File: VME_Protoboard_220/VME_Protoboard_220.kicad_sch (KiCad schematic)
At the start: 55 parts, among them J1 Conn_02x08_Odd_Even, J2 Conn_02x08_Odd_Even, J3 Conn_02x12_Odd_Even, J4 Conn_02x07_Odd_Even, U1 74x16245, U2 74x16245, U3 74x16245, U4 74x1G19, U5 74x1G07, U6 74x1G07, U7 74x1G125, U8 74x1G125, U9 74x1G125, X1 DIN41612_03x32_ABC_VMEbus

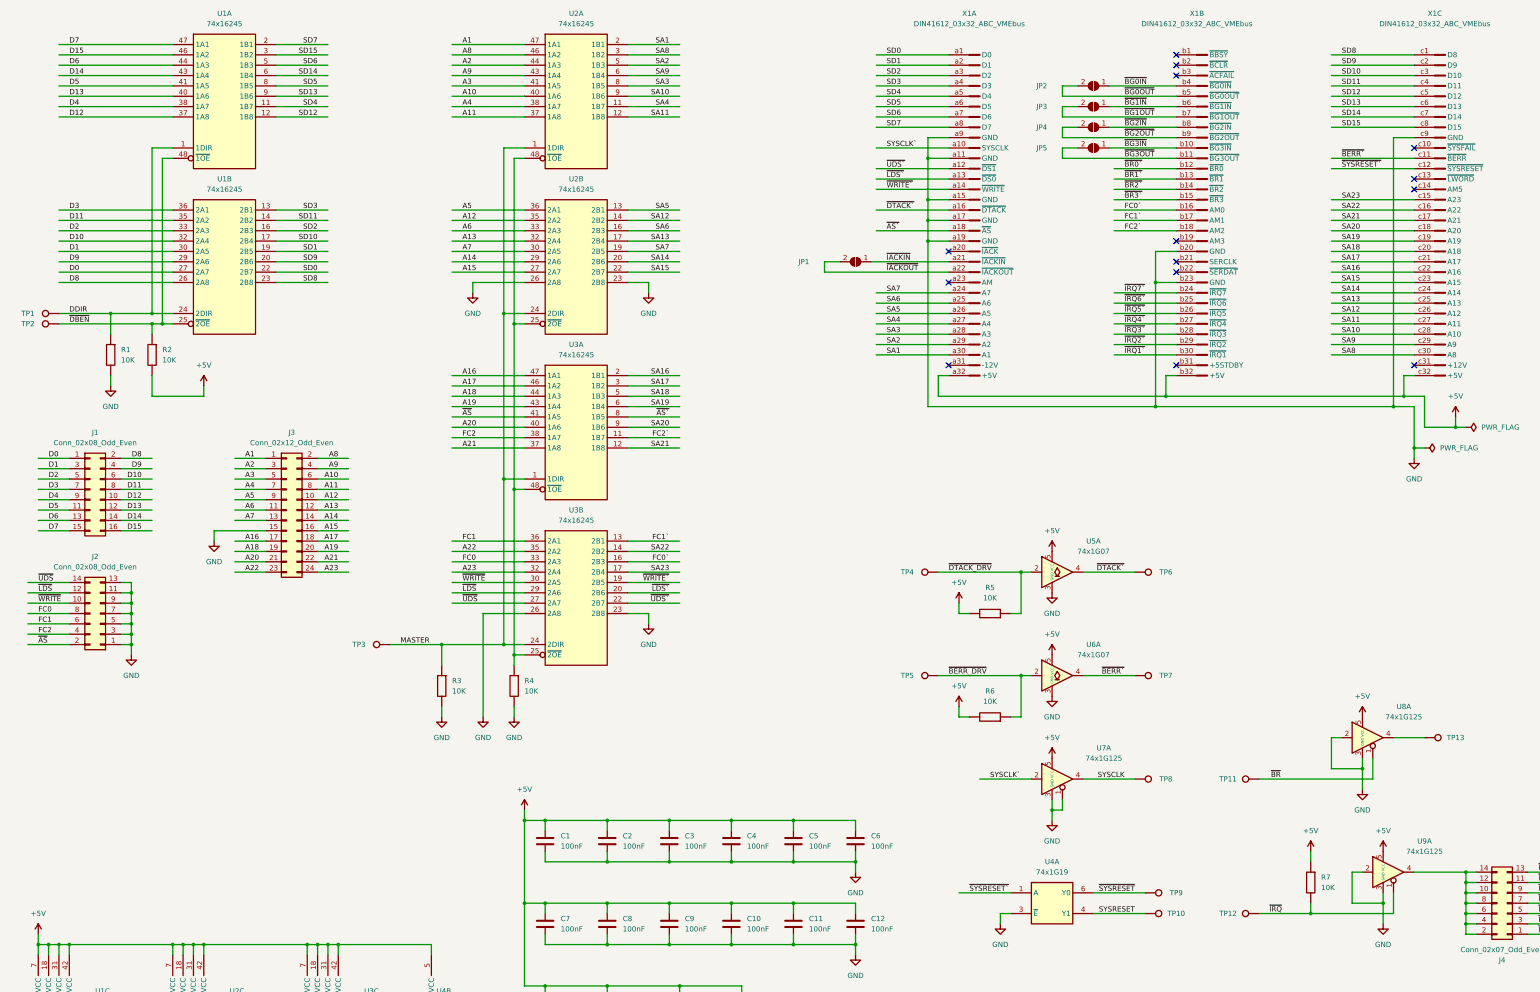
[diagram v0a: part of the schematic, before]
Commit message: Add extra test point for independent output control of each half of the data bus
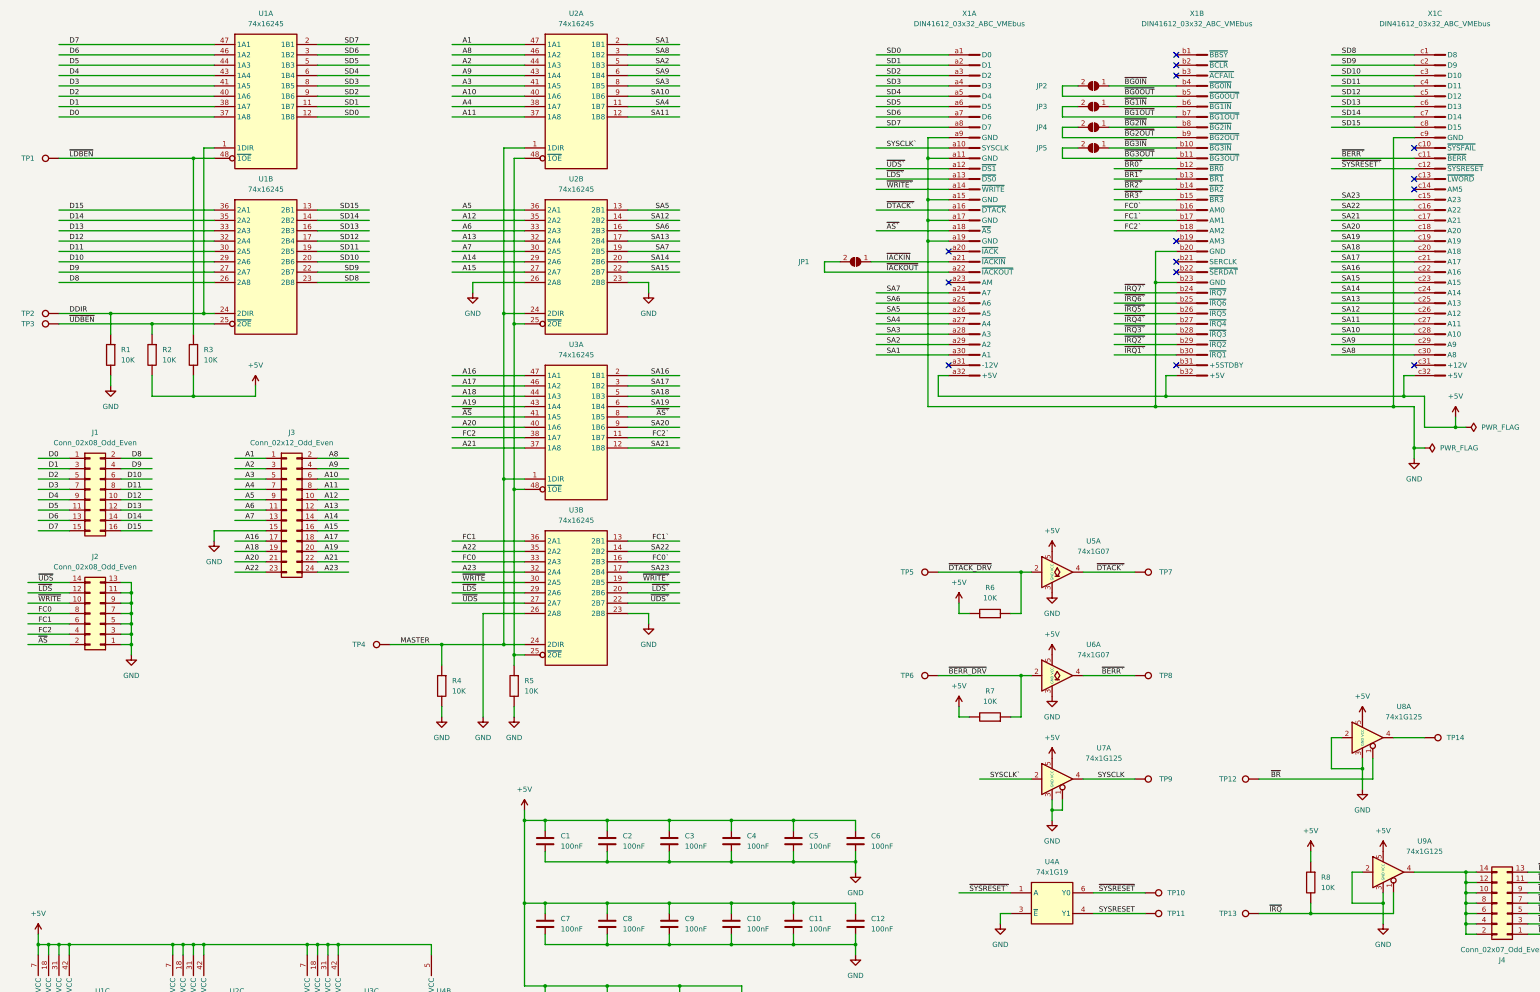
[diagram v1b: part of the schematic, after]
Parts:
- added R2: 10K, COMET_footprints:R_SMD0805, symbol COMET_symbols:R
- added TP1: TestPoint, TestPoint:TestPoint_Loop_D1.80mm_Drill1.0mm_Beaded, symbol Connector:TestPoint
- renumbered R2 to R3, R3 to R4, R4 to R5, R5 to R6, R6 to R7, R7 to R8, TP9 to TP10, TP10 to TP11, TP11 to TP12, TP12 to TP13, TP13 to TP14, TP1 to TP2, TP2 to TP3, TP3 to TP4, TP4 to TP5, TP5 to TP6, TP6 to TP7, TP7 to TP8, TP8 to TP9
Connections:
- net +5V: now also R2.1
- net D0: now also U1.37 (1A8); no longer U1.27 (2A7)
- net D1: now also U1.38 (1A7); no longer U1.30 (2A5)
- net D10: now also U1.29 (2A6); no longer U1.32 (2A4)
- net D11: now also U1.30 (2A5); no longer U1.35 (2A2)
- net D12: now also U1.32 (2A4); no longer U1.37 (1A8)
- net D13: now also U1.33 (2A3); no longer U1.40 (1A6)
- net D14: now also U1.35 (2A2); no longer U1.43 (1A4)
- net D15: now also U1.36 (2A1); no longer U1.46 (1A2)
- net D2: now also U1.40 (1A6); no longer U1.33 (2A3)
- net D3: now also U1.41 (1A5); no longer U1.36 (2A1)
- net D4: now also U1.43 (1A4); no longer U1.38 (1A7)
- net D5: now also U1.44 (1A3); no longer U1.41 (1A5)
- net D6: now also U1.46 (1A2); no longer U1.44 (1A3)
- net D9: now also U1.27 (2A7); no longer U1.29 (2A6)
- net SD0: now also U1.12 (1B8); no longer U1.22 (2B7)
- net SD1: now also U1.11 (1B7); no longer U1.19 (2B5)
- net SD10: now also U1.20 (2B6); no longer U1.17 (2B4)
- net SD11: now also U1.19 (2B5); no longer U1.14 (2B2)
- net SD12: now also U1.17 (2B4); no longer U1.12 (1B8)
- net SD13: now also U1.16 (2B3); no longer U1.9 (1B6)
- net SD14: now also U1.14 (2B2); no longer U1.6 (1B4)
- net SD15: now also U1.13 (2B1); no longer U1.3 (1B2)
- net SD2: now also U1.9 (1B6); no longer U1.16 (2B3)
- net SD3: now also U1.8 (1B5); no longer U1.13 (2B1)
- net SD4: now also U1.6 (1B4); no longer U1.11 (1B7)
- net SD5: now also U1.5 (1B3); no longer U1.8 (1B5)
- net SD6: now also U1.3 (1B2); no longer U1.5 (1B3)
- net SD9: now also U1.22 (2B7); no longer U1.20 (2B6)
- net ~{DBEN} renamed ~{LDBEN}
- net ~{LDBEN}: now also TP1.1; no longer TP3.1, U1.25 (~{2OE})
- new net ~{UDBEN}: R2.2, TP3.1, U1.25 (~{2OE})
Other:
- moved on the sheet: R3, U1A, U1B
